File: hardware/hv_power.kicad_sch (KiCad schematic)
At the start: 0 parts

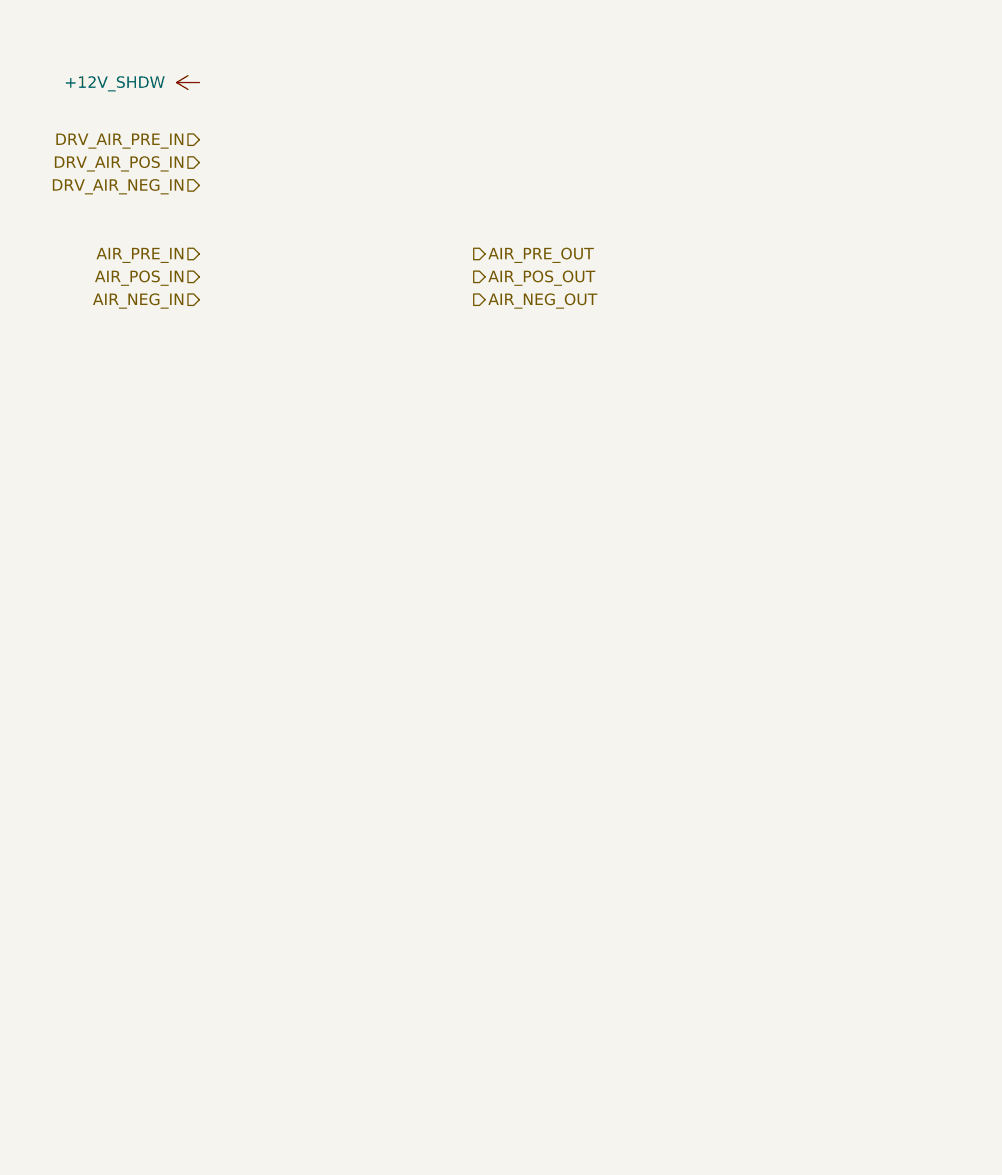
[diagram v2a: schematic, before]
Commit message: import relay package; add relays and precharge resistor to hv_power block; add flywheel protections to lv_relay_drive block
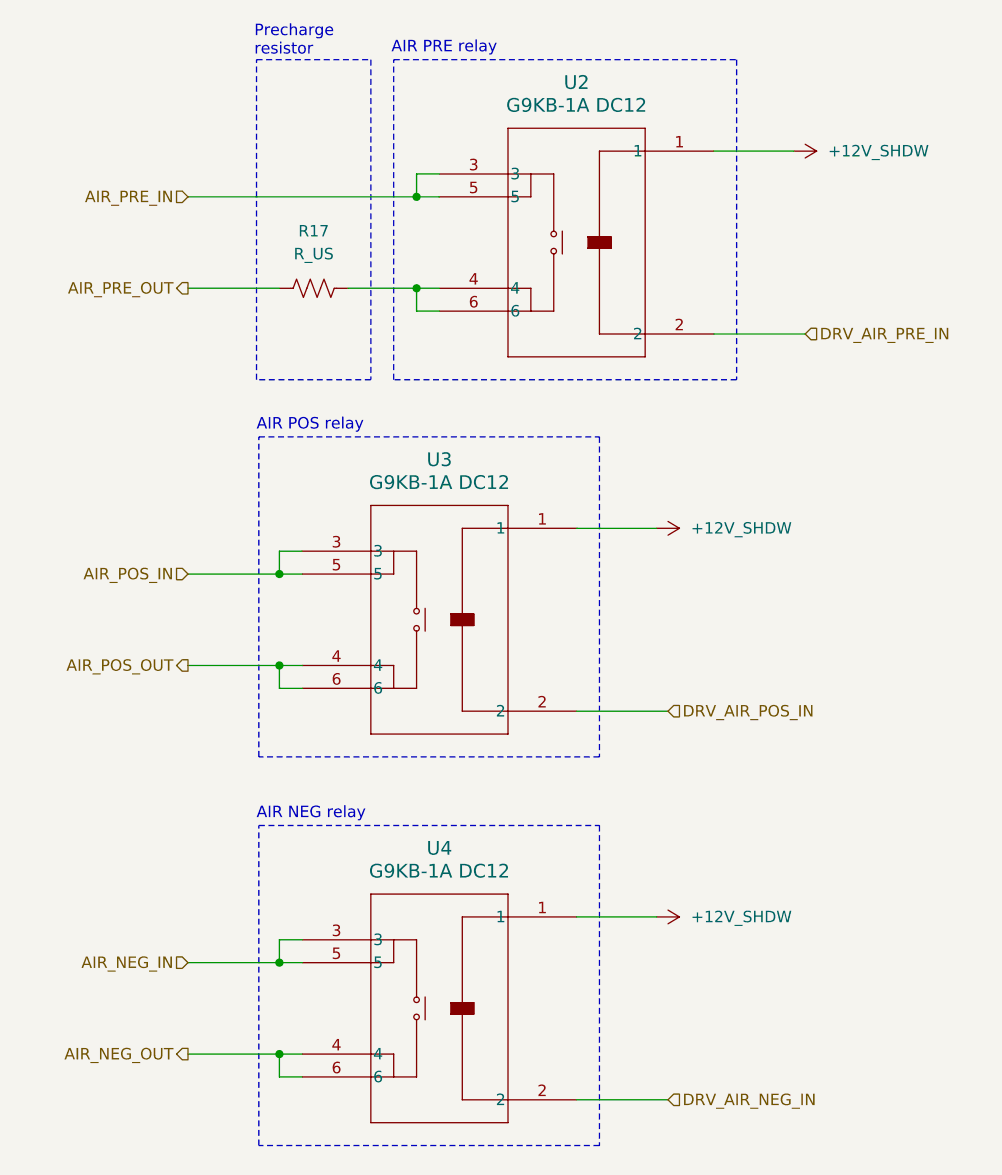
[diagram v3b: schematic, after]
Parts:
- added R17: R_US, symbol Device:R_US
- added U2, U3, U4: G9KB-1A DC12, RELAY_G9KB-1A_OMR, symbol G9KB_1A12V:G9KB-1A_DC12
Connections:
- net +12V_SHDW: now also U2.1, U3.1, U4.1
- net AIR_NEG_IN: now also U4.3, U4.5
- net AIR_NEG_OUT: now also U4.4, U4.6
- net AIR_POS_IN: now also U3.3, U3.5
- net AIR_POS_OUT: now also U3.4, U3.6
- net AIR_PRE_IN: now also U2.3, U2.5
- net AIR_PRE_OUT: now also R17.1
- net DRV_AIR_NEG_IN: now also U4.2
- net DRV_AIR_POS_IN: now also U3.2
- net DRV_AIR_PRE_IN: now also U2.2
- new net: R17.2, U2.4, U2.6
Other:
- note added: "AIR NEG relay"
- note added: "AIR POS relay"
- note added: "AIR PRE relay"
- note added: "Precharge resistor"

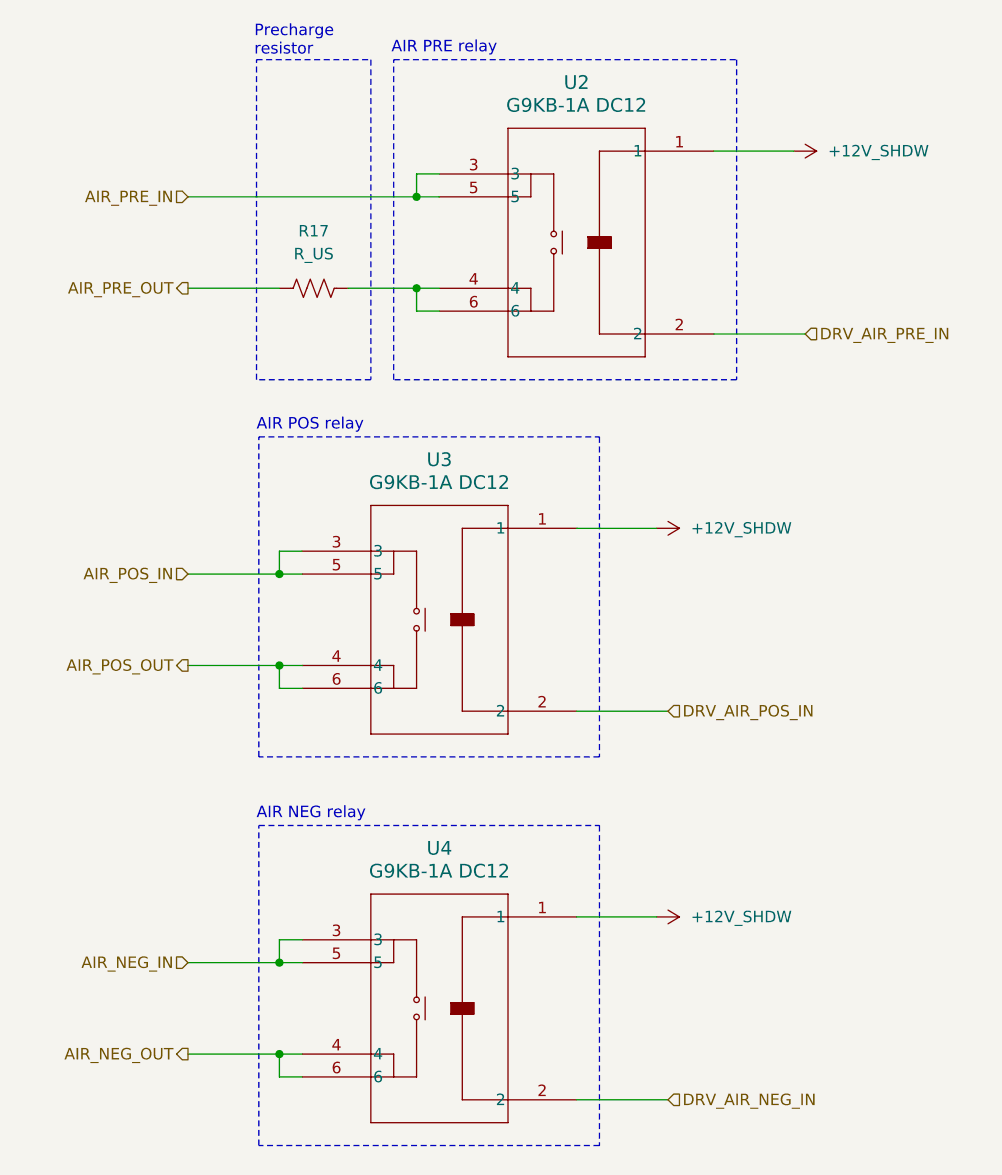
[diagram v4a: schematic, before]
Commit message: add full galvanic isoltation and comparator to hv_sense block
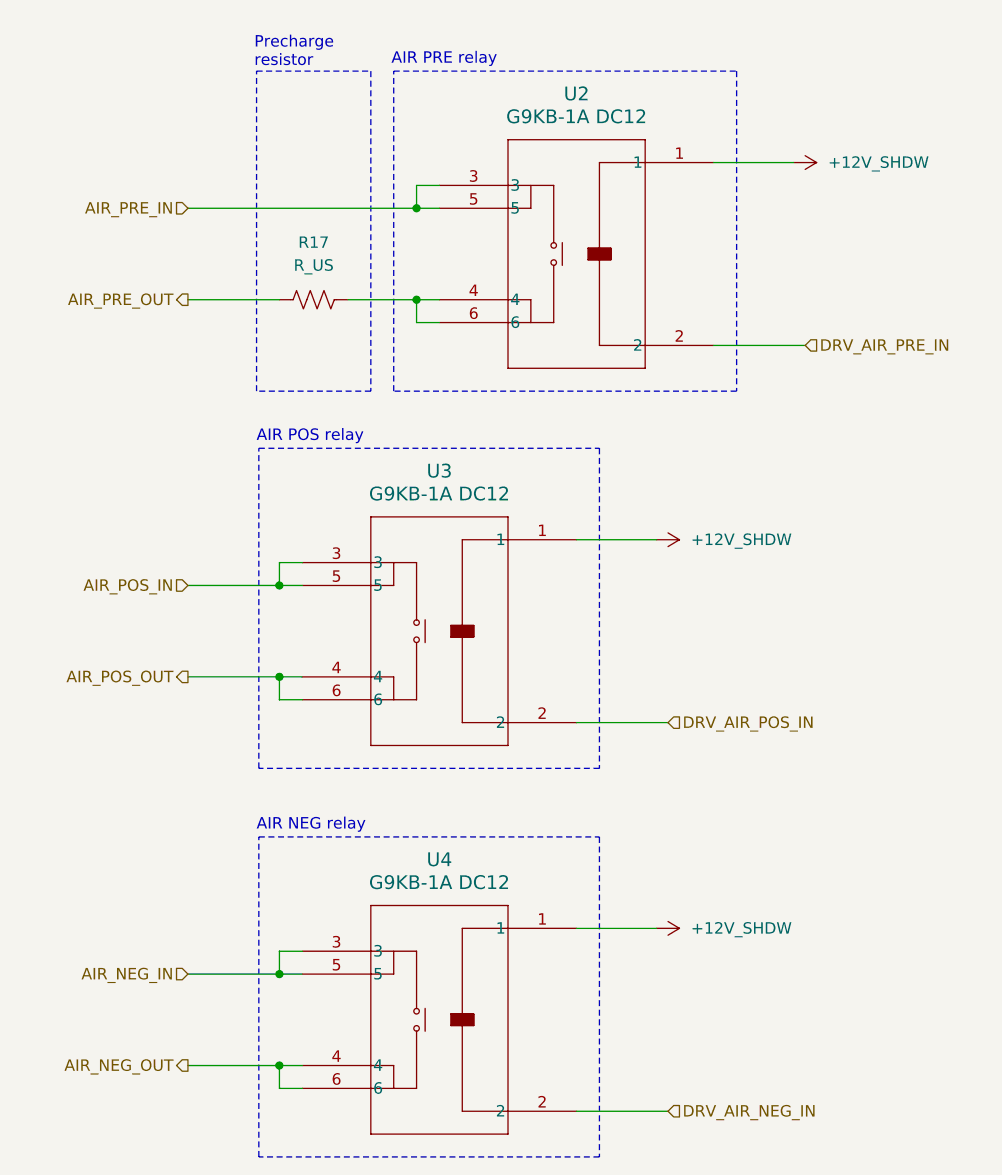
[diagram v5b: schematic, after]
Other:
- moved on the sheet: R17, U2, U3, U4

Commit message: start power supply and logic sizing
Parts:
- U2, U3, U4: footprint RELAY_G9KB-1A_OMR -> G9KB_Parts:G9KB_1A12V
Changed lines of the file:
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@@
 			)
 		)
-		(property "Footprint" "RELAY_G9KB-1A_OMR"
+		(property "Footprint" "G9KB_Parts:G9KB_1A12V"
 			(at 95.25 35.56 0)
 			(hide yes)
@@
 			)
 		)
-		(property "Footprint" "RELAY_G9KB-1A_OMR"
+		(property "Footprint" "G9KB_Parts:G9KB_1A12V"
 			(at 80.01 120.65 0)
 			(hide yes)
@@
 			)
 		)
-		(property "Footprint" "RELAY_G9KB-1A_OMR"
+		(property "Footprint" "G9KB_Parts:G9KB_1A12V"
 			(at 80.01 77.47 0)
 			(hide yes)
